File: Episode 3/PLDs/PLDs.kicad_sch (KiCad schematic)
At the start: 5 parts, among them J1 5V DC

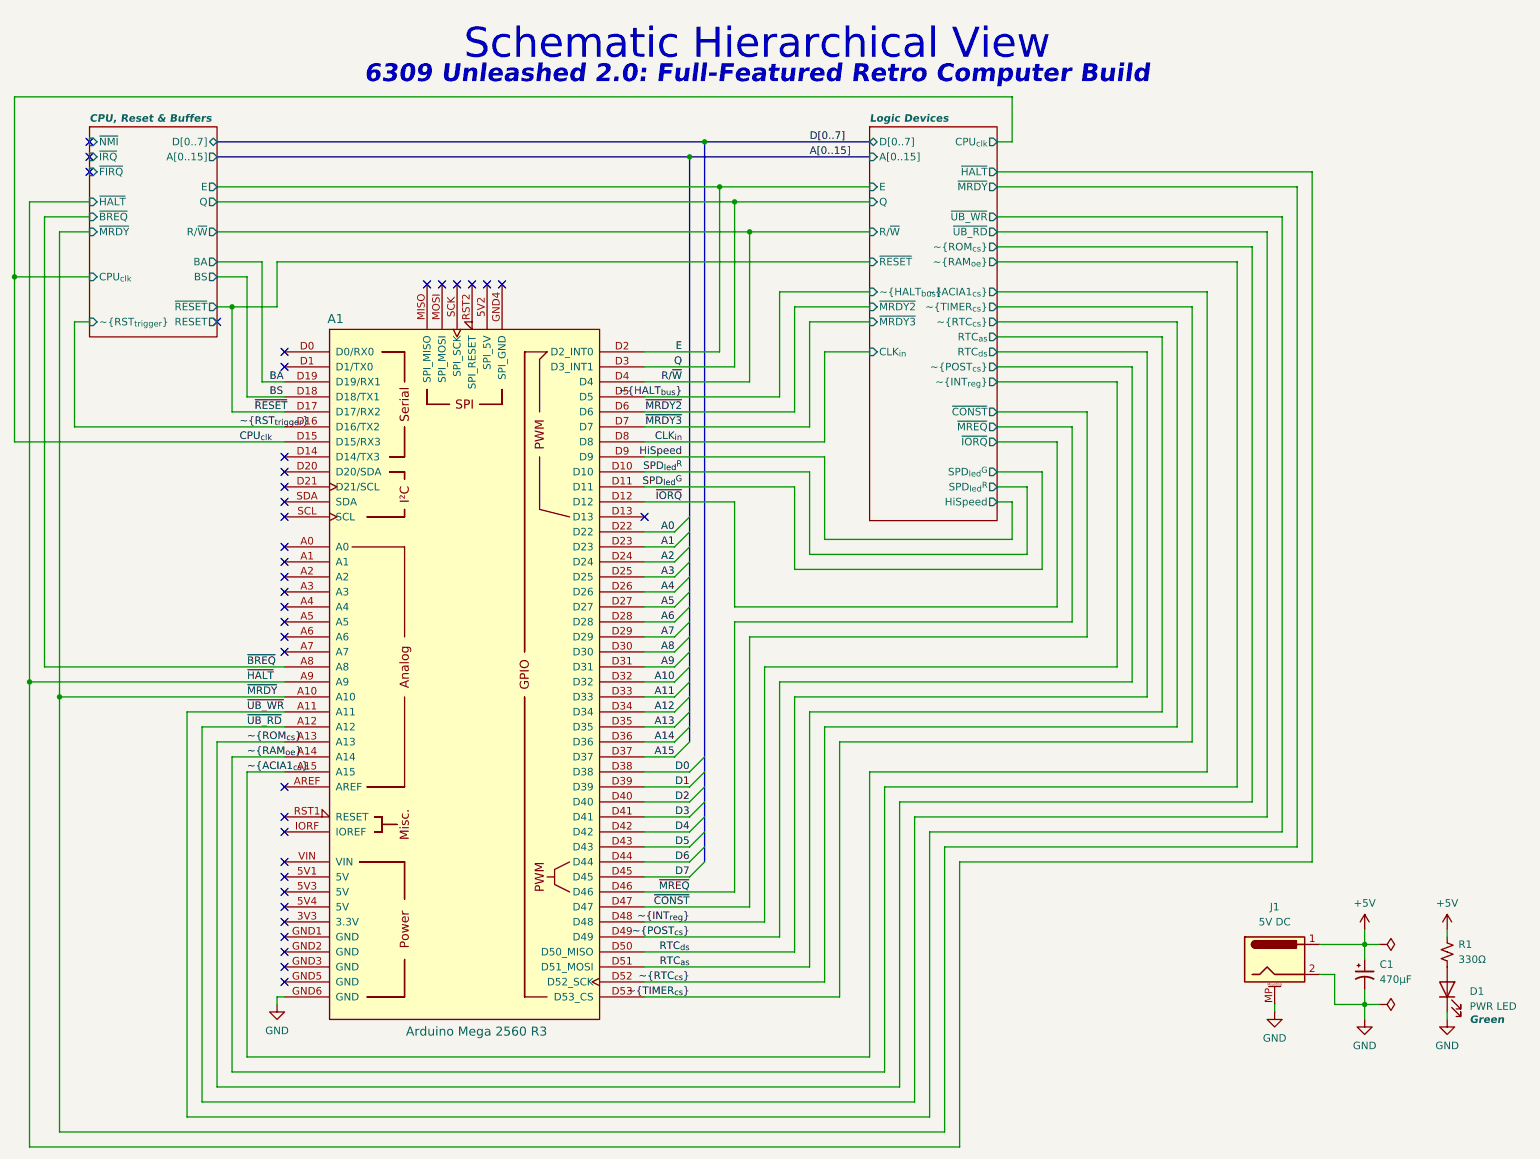
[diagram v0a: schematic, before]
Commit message: Updating PLD pin  assignments
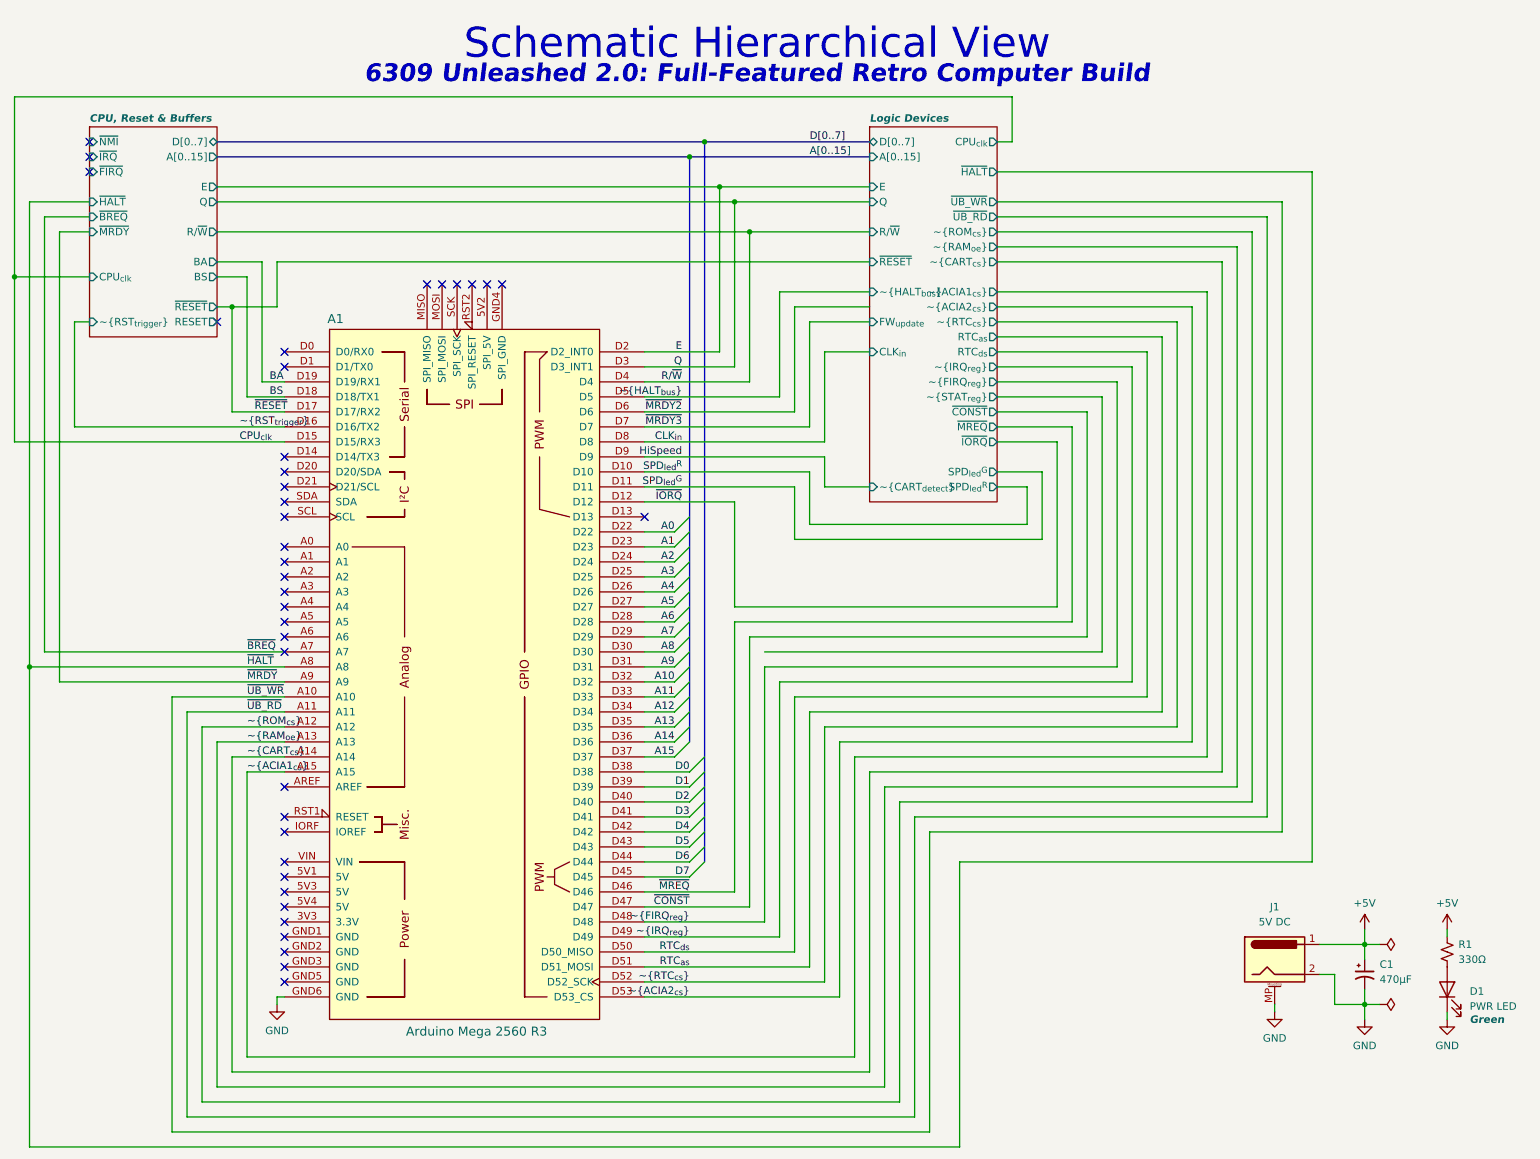
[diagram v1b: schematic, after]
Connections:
- net ~{BREQ}: now also A1.A7; no longer A1.A8
- net ~{HALT}: now also A1.A8; no longer A1.A9
- net ~{MRDY}: now also A1.A9; no longer A1.A10
- net ~{RAM_{oe}}: now also A1.A13; no longer A1.A14
- net ~{ROM_{cs}}: now also A1.A12; no longer A1.A13
- net ~{UB_RD}: now also A1.A11; no longer A1.A12
- net ~{UB_WR}: now also A1.A10; no longer A1.A11
- net ~{INT_{reg}} renamed ~{FIRQ_{reg}}
- net ~{POST_{cs}} renamed ~{IRQ_{reg}}
- net ~{TIMER_{cs}} renamed ~{ACIA2_{cs}}
- new net ~{CART_{cs}}: A1.A14
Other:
- sheet Logic Devices ports: added FW_{update}, ~{ACIA2_{cs}}, ~{CART_{cs}}, ~{CART_{detect}}, ~{FIRQ_{reg}}, ~{IRQ_{reg}}, ~{STAT_{reg}}; removed HiSpeed, ~{INT_{reg}}, ~{MRDY2}, ~{MRDY3}, ~{MRDY}, ~{POST_{cs}}, ~{TIMER_{cs}}
